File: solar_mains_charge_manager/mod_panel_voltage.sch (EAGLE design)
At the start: 31 parts, among them IC1 ACS750LCA-050, T1 TIP122, X10 22-23-2041, X2 22-23-2021, X3 22-23-2031, X5 22-23-2031, X6 22-23-2041, X7 53047-15, X8 53047-15

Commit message: A lot of stuff
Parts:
- removed D1, D2, D3, D4: 1N4004, diode:1N4004
- removed D5, D6: (no value), diode:ZENER-DIODEDO34-7
- removed IC1: ACS750LCA-050, allegro:ACS750LCA-050
- removed OK1, OK2: PC817, optocoupler:PC817
- removed R1, R11, R2, R3, R4, R5: (no value), resistor:R-EU_0204/5
- removed R6, R7: (no value), resistor:R-EU_0204/7
- removed T1: TIP122, transistor:TIP122
- removed U$1: NANO, Arduino-clone:NANO
- removed X10, X6: 22-23-2041, con-molex:22-23-2041
- removed X2: 22-23-2021, con-molex:22-23-2021
- removed X3, X5: 22-23-2031, con-molex:22-23-2031
- removed X7, X8: 53047-15, con-molex:53047-15
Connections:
- removed net 12V: OK1.COL, U$1.RAW, X2-1.S, X5-3.S, X7-1.S
- removed net BAT: R1.1, X10-2.S, X5-2.S
- removed net N$1: U$1.3.3V, U$1.AREF, X7-13.S, X7-14.S
- removed net N$11: D1.C, D2.C, R7.2
- removed net N$12: OK2.COL, U$1.D12, X8-1.S
- removed net N$13: D1.A, D3.C
- removed net N$15: D2.A, D4.C, R6.1
- removed net N$16: R6.2
- removed net N$17: U$1.D11, X3-2.S, X8-2.S
- removed net N$18: U$1.D10, X3-3.S, X8-3.S
- removed net N$19: U$1.D9, X6-3.S, X8-4.S
- removed net N$2: R3.2, U$1.D13, X7-15.S
- removed net N$20: U$1.D8, X6-4.S, X8-5.S
- removed net N$21: U$1.RST, X6-2.S, X7-3.S
- removed net N$22: U$1.D7, X8-6.S
- removed net N$23: U$1.D6, X8-7.S
- removed net N$24: U$1.D5, X8-8.S
- removed net N$25: U$1.D4, X8-9.S
- removed net N$26: U$1.D3, X8-10.S
- removed net N$27: U$1.D2, X8-11.S
- removed net N$28: U$1.GND2, X8-12.S
- removed net N$29: U$1.RST1, X8-13.S
- removed net N$30: U$1.RX1, X8-14.S
- removed net N$31: U$1.TX0, X8-15.S
- removed net N$32: U$1.5.5V, X7-4.S
- removed net N$33: U$1.A7, X7-5.S
- removed net N$34: U$1.A6, X7-6.S
- removed net N$35: U$1.A5, X7-7.S
- removed net N$36: U$1.A4, X7-8.S
- removed net N$37: U$1.A3, X7-9.S
- removed net N$38: U$1.A2, X7-10.S
- removed net N$4: OK1.A, R3.1
- removed net N$40: D6.C, R11.2, U$1.A0, X7-12.S
- removed net N$43: R1.2, R11.1, R2.2
- removed net N$5: T1.C, X2-2.S
- removed net N$6: OK1.EMIT, R4.1
- removed net N$7: R4.2, T1.B
- removed net N$8: D3.A, D4.A, D5.A, OK2.C, R5.1
- removed net N$9: D5.C, OK2.A, R5.2, R7.1
- net GND: no longer D6.A, OK1.C, OK2.EMIT, R2.1, T1.E, U$1.GND, X10-1.S, X3-1.S, X5-1.S, X6-1.S, X7-2.S
- net N$39: no longer U$1.A1, X7-11.S
- net N$41: no longer X10-4.S
- net N$42: no longer X10-3.S
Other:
- moved on the sheet: D7, D8, R10, R12, R9

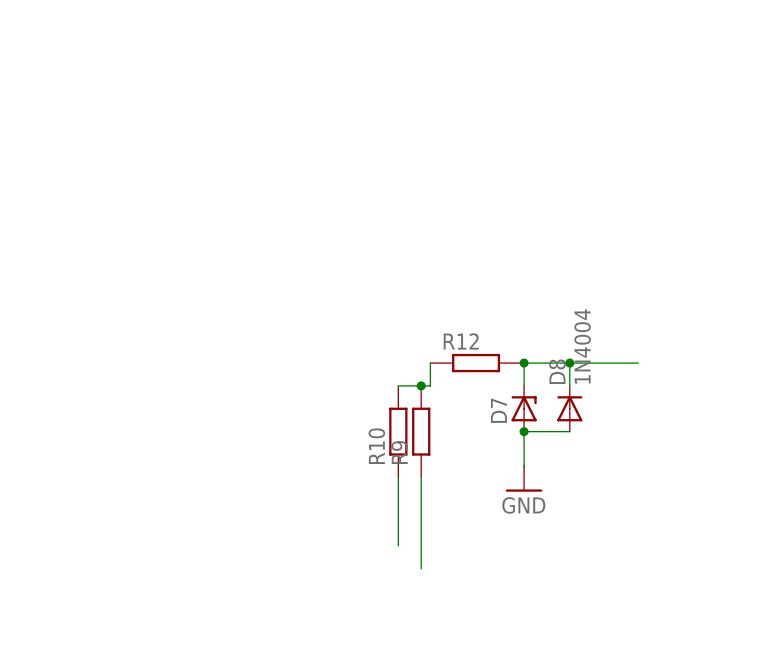
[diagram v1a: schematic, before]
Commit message: Finished board layout of mod_switch_battery_voltage and more work on psu_considerations.ods
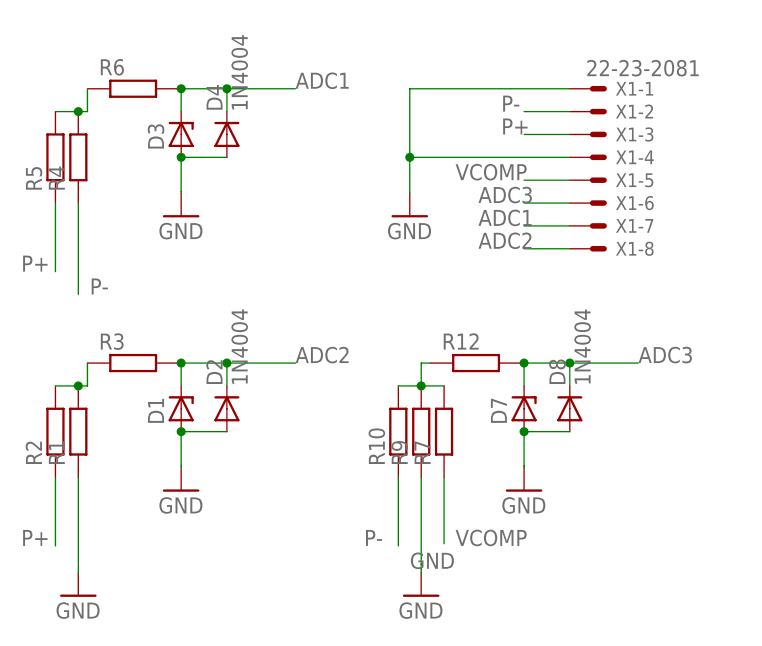
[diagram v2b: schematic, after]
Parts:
- added D1, D3: (no value), diode:ZENER-DIODEDO34-7
- added D2, D4: 1N4004, diode:1N4004
- added R1, R2, R3, R4, R5, R6, R7: (no value), resistor:R-EU_0204/5
- added X1: 22-23-2081, con-molex:22-23-2081
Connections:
- removed net N$3: R10.2, R12.1, R9.2
- removed net N$39: D7.C, D8.C, R12.2
- removed net N$41: R10.1
- removed net N$42: R9.1
- new net ADC1: D3.C, D4.C, R6.2, X1-7.S
- new net ADC2: D1.C, D2.C, R3.2, X1-8.S
- new net ADC3: D7.C, D8.C, R12.2, X1-6.S
- new net N$2: R10.2, R12.1, R7.2, R9.2
- new net N$5: R1.2, R2.2, R3.1
- new net N$9: R4.2, R5.2, R6.1
- new net P+: R2.1, R5.1, X1-3.S
- new net P-: R10.1, R4.1, X1-2.S
- new net VCOMP: R7.1, X1-5.S
- net GND: now also D1.A, D2.A, D3.A, D4.A, R1.1, R9.1, X1-1.S, X1-4.S
